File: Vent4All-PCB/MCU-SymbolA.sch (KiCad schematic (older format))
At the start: 3 parts, among them U1 NUCLEO-F429ZI

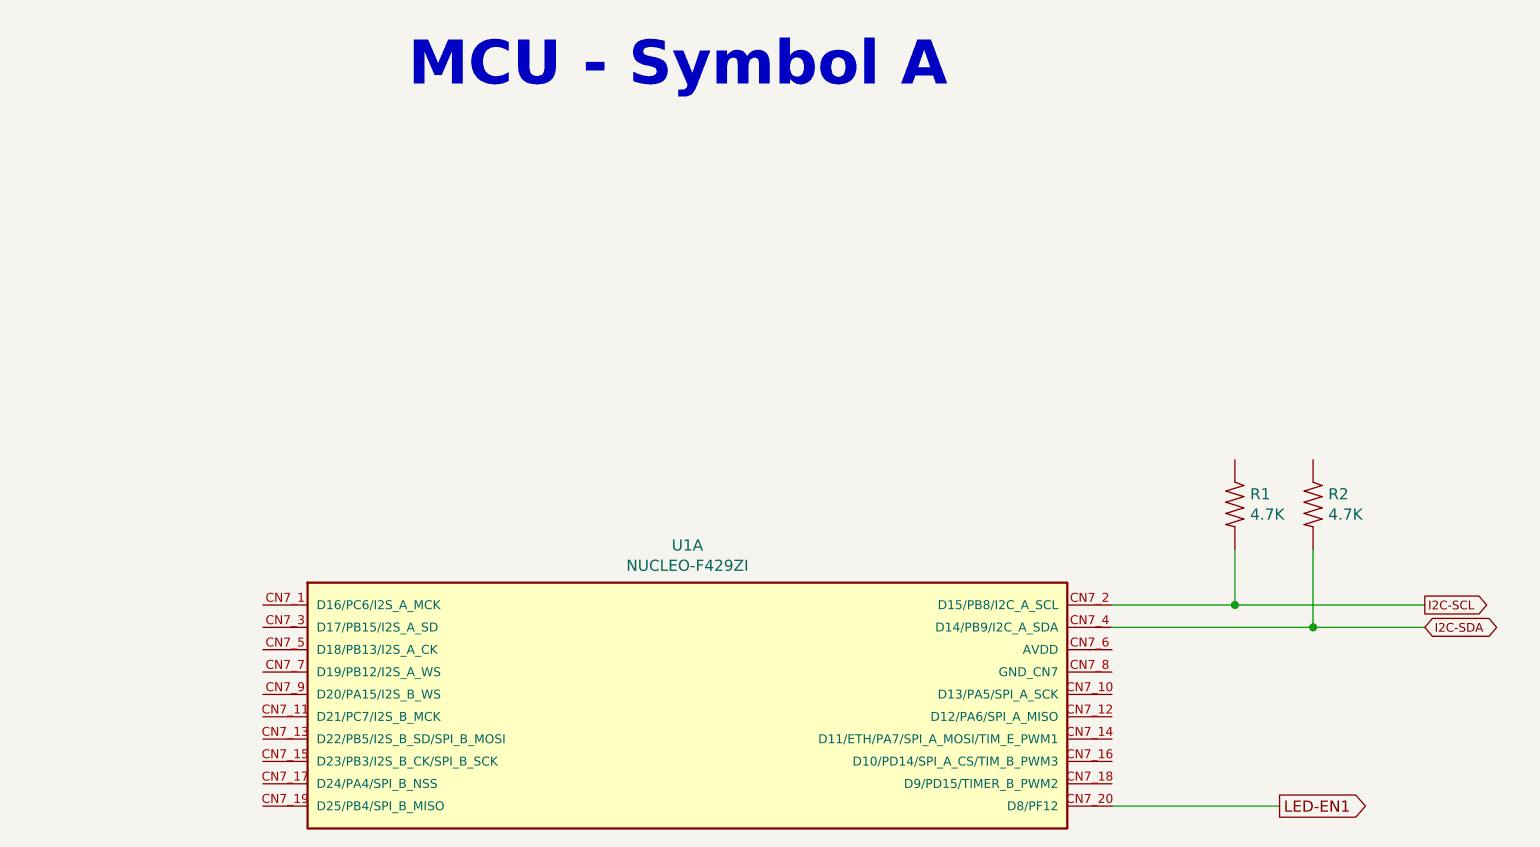
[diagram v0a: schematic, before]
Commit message: Added global labels for reserved communication lines (SPI, I2C, UARTs).
Added hierarchical sheet for external connection interfaces (e.g. to RPi).
Changed symbol libraries table to use ${KIPRJMOD} instead of absolute paths.
When I imported the schematic, KiCAD made a rescue library and changed the line endings of all the .sch files.
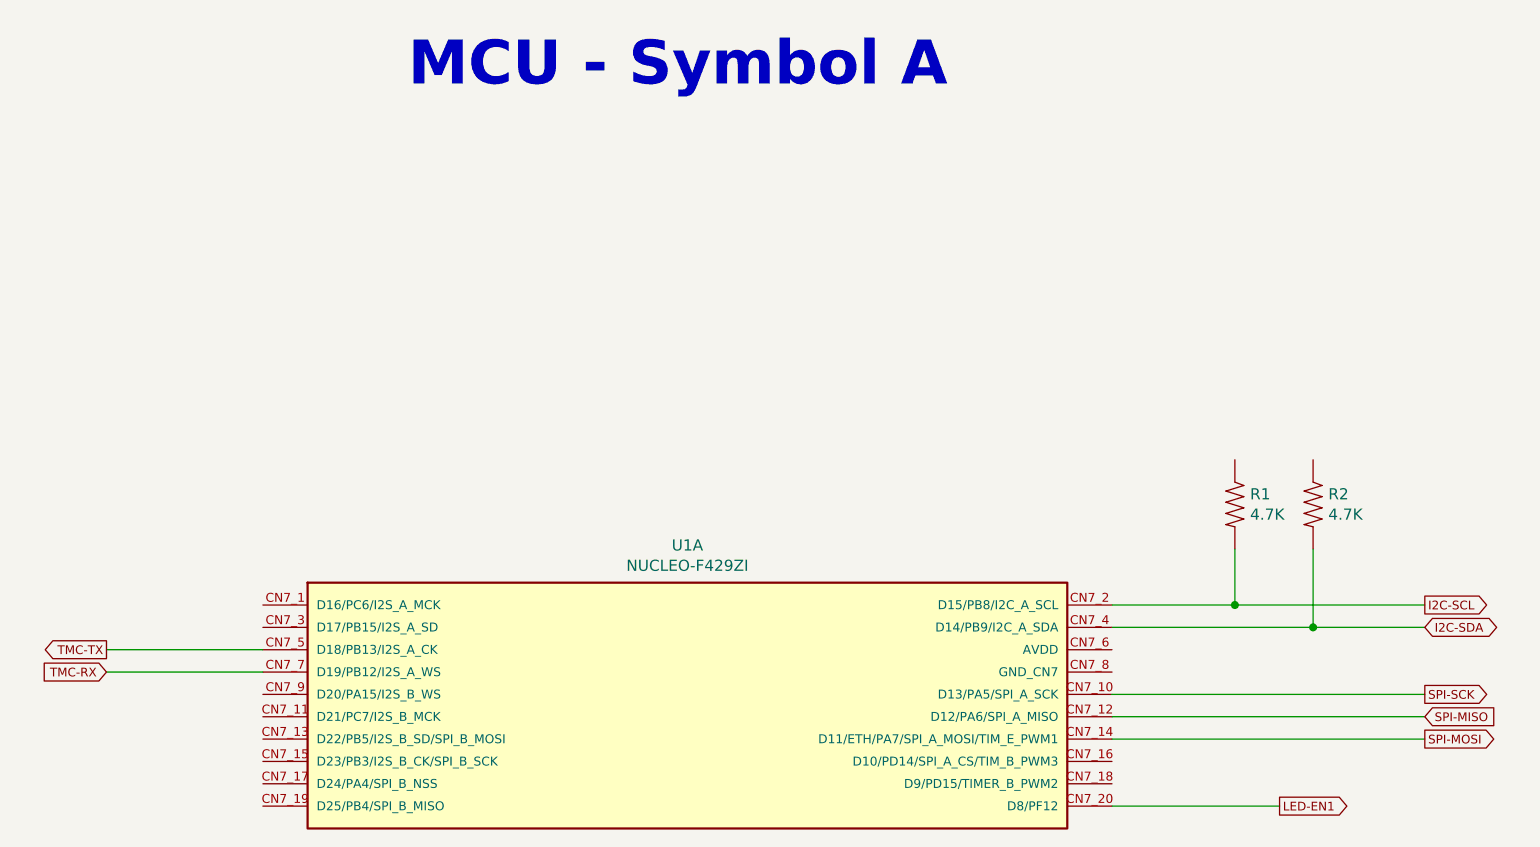
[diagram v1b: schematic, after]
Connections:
- net SPI-SCK: now reaches U1.CN7_10 (D13/PA5/SPI_A_SCK)
- net SPI-MISO: now reaches U1.CN7_12 (D12/PA6/SPI_A_MISO)
- net SPI-MOSI: now reaches U1.CN7_14 (D11/ETH/PA7/SPI_A_MOSI/TIM_E_PWM1)
- net TMC-TX: now reaches U1.CN7_5 (D18/PB13/I2S_A_CK)
- net TMC-RX: now reaches U1.CN7_7 (D19/PB12/I2S_A_WS)
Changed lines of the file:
@@
 Text Notes 4350 1150 0    197  ~ 39
 MCU - Symbol A
-Wire Wire Line
-	8900 3450 8050 3450
-Text GLabel 8900 3450 2    39   Output ~ 0
-I2C-SCL
 Text GLabel 8900 3550 2    39   BiDi ~ 0
 I2C-SDA
@@
 	8050 3200 8050 3450
 Connection ~ 8050 3450
-Wire Wire Line
-	8050 3450 7500 3450
 $Comp
 L Vent4All_Library:RESISTOR0603 R1
@@
 Wire Wire Line
 	8250 4350 7500 4350
-Text GLabel 8250 4350 2    50   Output ~ 0
+Text GLabel 8250 4350 2    39   Output ~ 0
 LED-EN1
+Wire Wire Line
+	3700 3650 3000 3650
+Text GLabel 3000 3750 0    39   Input ~ 0
+TMC-RX
+Text GLabel 3000 3650 0    39   Output ~ 0
+TMC-TX
+Wire Wire Line
+	3000 3750 3700 3750
+Text GLabel 8900 3850 2    39   Output ~ 0
+SPI-SCK
+Wire Wire Line
+	8900 3850 7500 3850
+Text GLabel 8900 3950 2    39   Input ~ 0
+SPI-MISO
+Wire Wire Line
+	8900 3950 7500 3950
+Text GLabel 8900 4050 2    39   Output ~ 0
+SPI-MOSI
+Wire Wire Line
+	8900 4050 7500 4050
+Wire Wire Line
+	8050 3450 7500 3450
+Wire Wire Line
+	8900 3450 8050 3450
+Text GLabel 8900 3450 2    39   Output ~ 0
+I2C-SCL
 $EndSCHEMATC

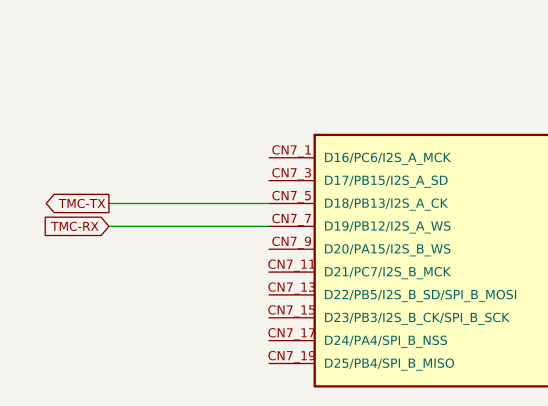
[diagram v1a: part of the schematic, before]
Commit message: Added schematic connections for HSC sensors.
Note: this assumes HSC sensors will be soldered directly to the PCB. If we are placing them on daughter boards then we will need to choose the pin header connectors and move the HSC symbols into a separate sheet.
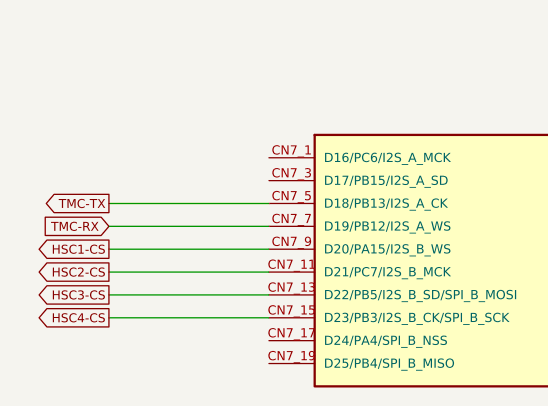
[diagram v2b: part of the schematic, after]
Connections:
- net HSC2-CS: now reaches U1.CN7_11 (D21/PC7/I2S_B_MCK)
- net HSC3-CS: now reaches U1.CN7_13 (D22/PB5/I2S_B_SD/SPI_B_MOSI)
- net HSC4-CS: now reaches U1.CN7_15 (D23/PB3/I2S_B_CK/SPI_B_SCK)
- net HSC1-CS: now reaches U1.CN7_9 (D20/PA15/I2S_B_WS)
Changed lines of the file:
@@
 Text GLabel 8900 3450 2    39   Output ~ 0
 I2C-SCL
+Text GLabel 3000 3850 0    39   Output ~ 0
+HSC1-CS
+Text GLabel 3000 3950 0    39   Output ~ 0
+HSC2-CS
+Text GLabel 3000 4050 0    39   Output ~ 0
+HSC3-CS
+Text GLabel 3000 4150 0    39   Output ~ 0
+HSC4-CS
+Wire Wire Line
+	3000 4150 3700 4150
+Wire Wire Line
+	3000 4050 3700 4050
+Wire Wire Line
+	3000 3950 3700 3950
+Wire Wire Line
+	3000 3850 3700 3850
 $EndSCHEMATC
